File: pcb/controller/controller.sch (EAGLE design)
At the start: 23 parts, among them SW1 EC12E_SW, U1 LCD-16X2NOHOLES

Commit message: Work on controller layout.
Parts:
- removed 3.3V: M01PTH, SparkFun-Connectors:M01PTH
- removed IO1, IO2: (no value), SparkFun-Connectors:M03PTH
- removed POWERLED: (no value), led:LEDSMT1206
- removed S1: CM4400, sensor-comus-group:CM4400
- added BLUETOOTH, JP1, JP2: (no value), SparkFun-Connectors:M041X04_NO_SILK
- added ETHERNET: M05X2NO_SILK, SparkFun-Connectors:M05X2NO_SILK
- added IC1: 74HCT595D, 74xx-eu:74HCT595D
- added JOYSTICK: (no value), SparkFun-Connectors:M05NO_SILK
- added L2: WS2812B, adafruit:WS2812B
- added R2: 1k, rcl:R-EU_M0805
- added R4: 2k, rcl:R-EU_M0805
- added S2, S3: SWITCH-MOMENTARY-2-SMD-1101NE, SparkFun-Electromechanical:SWITCH-MOMENTARY-2-SMD-1101NE
- added VIBRATION_SENSOR: M021X02_NO_SILK, SparkFun-Connectors:M021X02_NO_SILK
- R3: value 100R -> 470R
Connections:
- new net BLUETOOTH_RX: BLUETOOTH.1, R2.1, R4.2
- new net BLUETOOTH_TX: BLUETOOTH.2, U$1.RXI
- new net ETHERNET_CLOCK_OUT: ETHERNET.1
- new net ETHERNET_INT: ETHERNET.2
- new net ETHERNET_RESET: ETHERNET.8
- new net ETHERNET_SELECT: ETHERNET.7, U$1.4
- new net ETHERNET_WDL: ETHERNET.3
- new net LCD_SELECT: IC1A.RCK, U$1.2
- new net PIN3: U$1.*3
- new net PIN5: U$1.*5
- new net PIN6: U$1.*6
- new net PIN7: U$1.7
- new net SERIAL_CLOCK: ETHERNET.6, IC1A.SCK, U$1.13
- new net SERIAL_MISO: ETHERNET.4, U$1.12
- new net SERIAL_MOSI: ETHERNET.5, IC1A.SER, U$1.*11
- new net STATUS_LED2: L1.DOUT, L2.DIN
- net +3V3: now also ETHERNET.9, JP1.3, JP2.3, R3.2; no longer 3.3V.1, POWERLED.A
- net +5V: now also BLUETOOTH.4, IC1A.SCL, IC1P.VCC, JP1.4, JP2.4, L2.VDD; no longer IO1.3, IO2.3
- net EXTRA_IO1: now also JP1.2; no longer IO1.2
- net EXTRA_IO2: now also JP2.2; no longer IO2.2
- net GND: now also BLUETOOTH.3, ETHERNET.10, IC1A.G, IC1P.GND, JP1.1, JP2.1, L2.GND, R4.1, VIBRATION_SENSOR.1; no longer IO1.1, IO2.1, S1.1
- net LCD_DATA4: now also IC1A.QD; no longer U$1.4
- net LCD_DATA5: now also IC1A.QE; no longer U$1.*5
- net LCD_DATA6: now also IC1A.QF; no longer U$1.*6
- net LCD_DATA7: now also IC1A.QG; no longer U$1.7
- net LCD_ENABLE: now also IC1A.QC; no longer U$1.*3
- net LCD_RS: now also IC1A.QB; no longer U$1.2
- net LEDSTRIP_OUT: now also L2.DOUT; no longer L1.DOUT
- net N$1: now also R2.2, U$1.TXO; no longer POWERLED.C, R3.2
- net RADIO_MISO: no longer U$1.12
- net RADIO_MOSI: no longer U$1.*11
- net RADIO_SCK: no longer U$1.13
- net SHAKE_SENSOR: now also VIBRATION_SENSOR.2; no longer S1.2
- net V+: now also U$1.RAW
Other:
- note added: "Bluetooth"
- note added: "Ethernet"
- note added: "NOTE: The regulator needs at least a 10mA load to work, and the radio may draw less than that, so we add an additional pulldown resistor on the 3.3V power rail."
- note added: "Preview LED"
- note removed: "3.3V Out Pin"
- note removed: "NOTE: The regulator needs at least a 10mA load to work, and the radio may draw less than that, so we add the power led on the 3.3V rail."
- note removed: "Status LED"
- moved on the sheet: R1, R3, U1

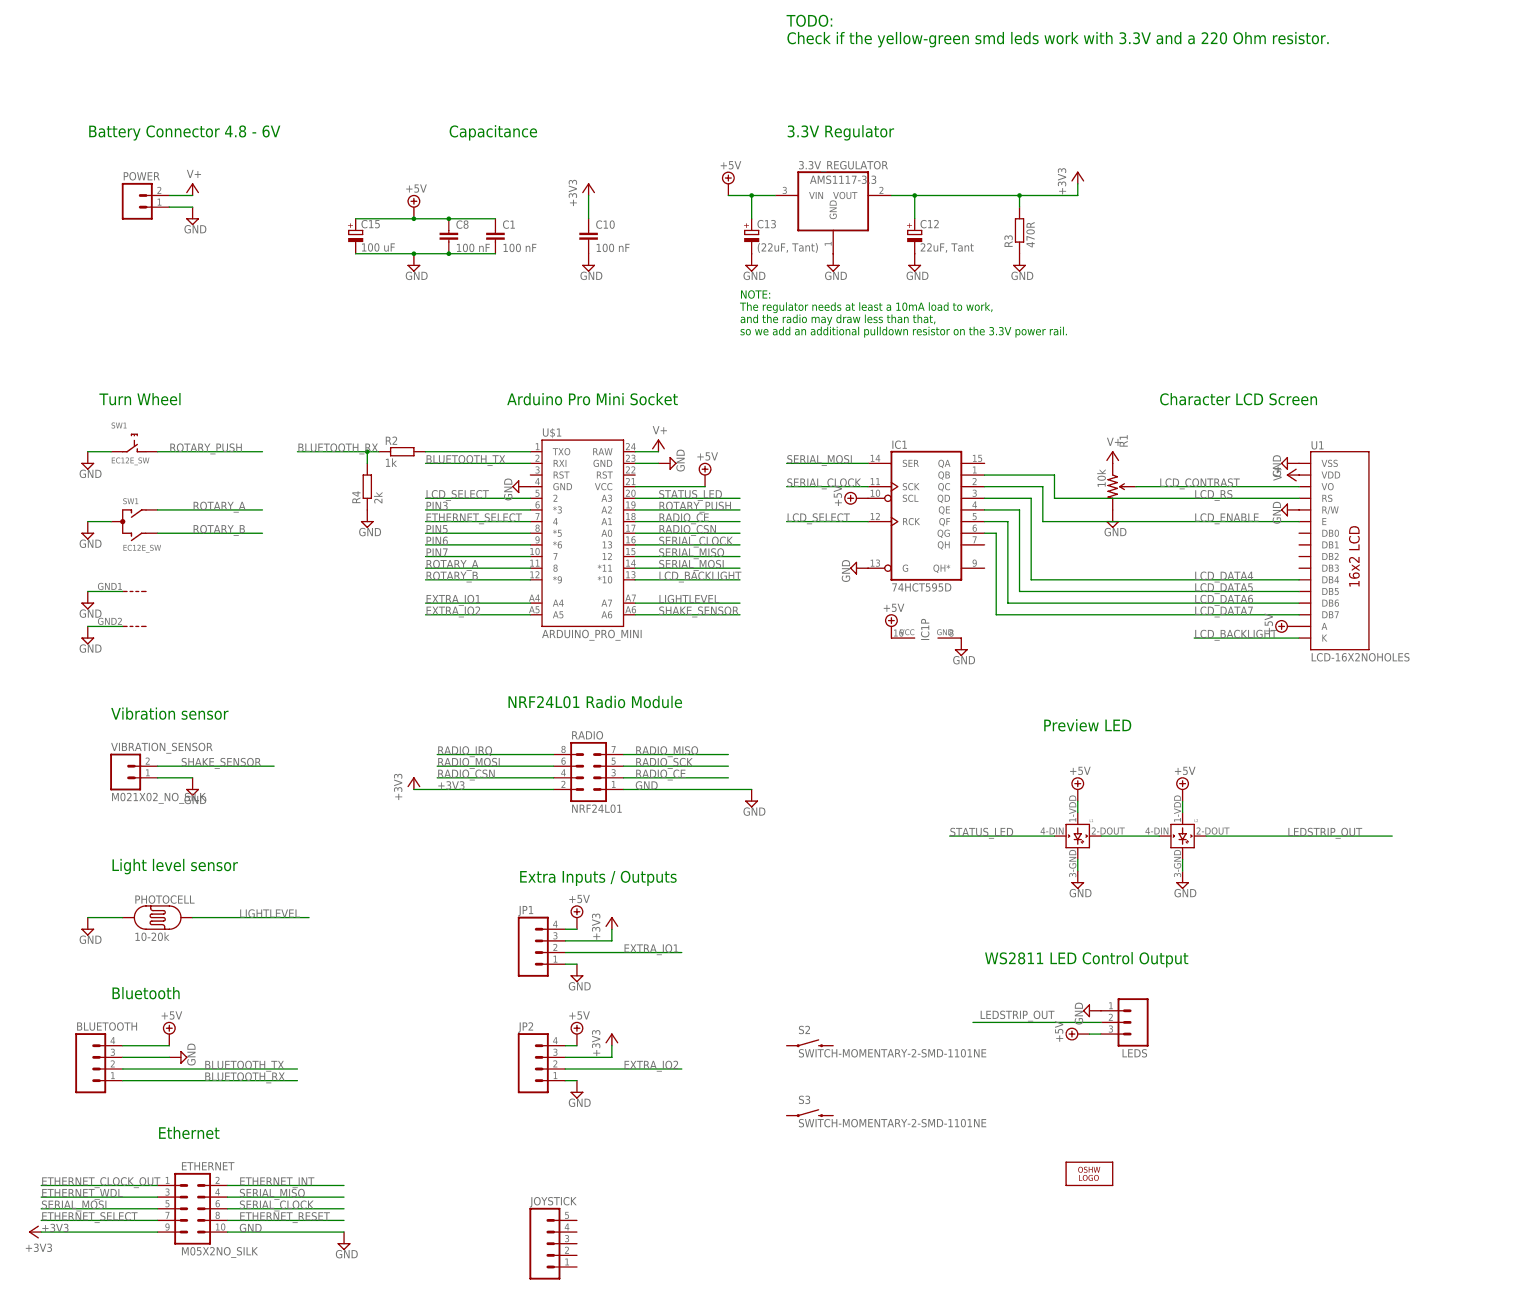
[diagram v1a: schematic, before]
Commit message: Working on remote controller pcb. Added library with connectors and outlines of some of the used third party modules.
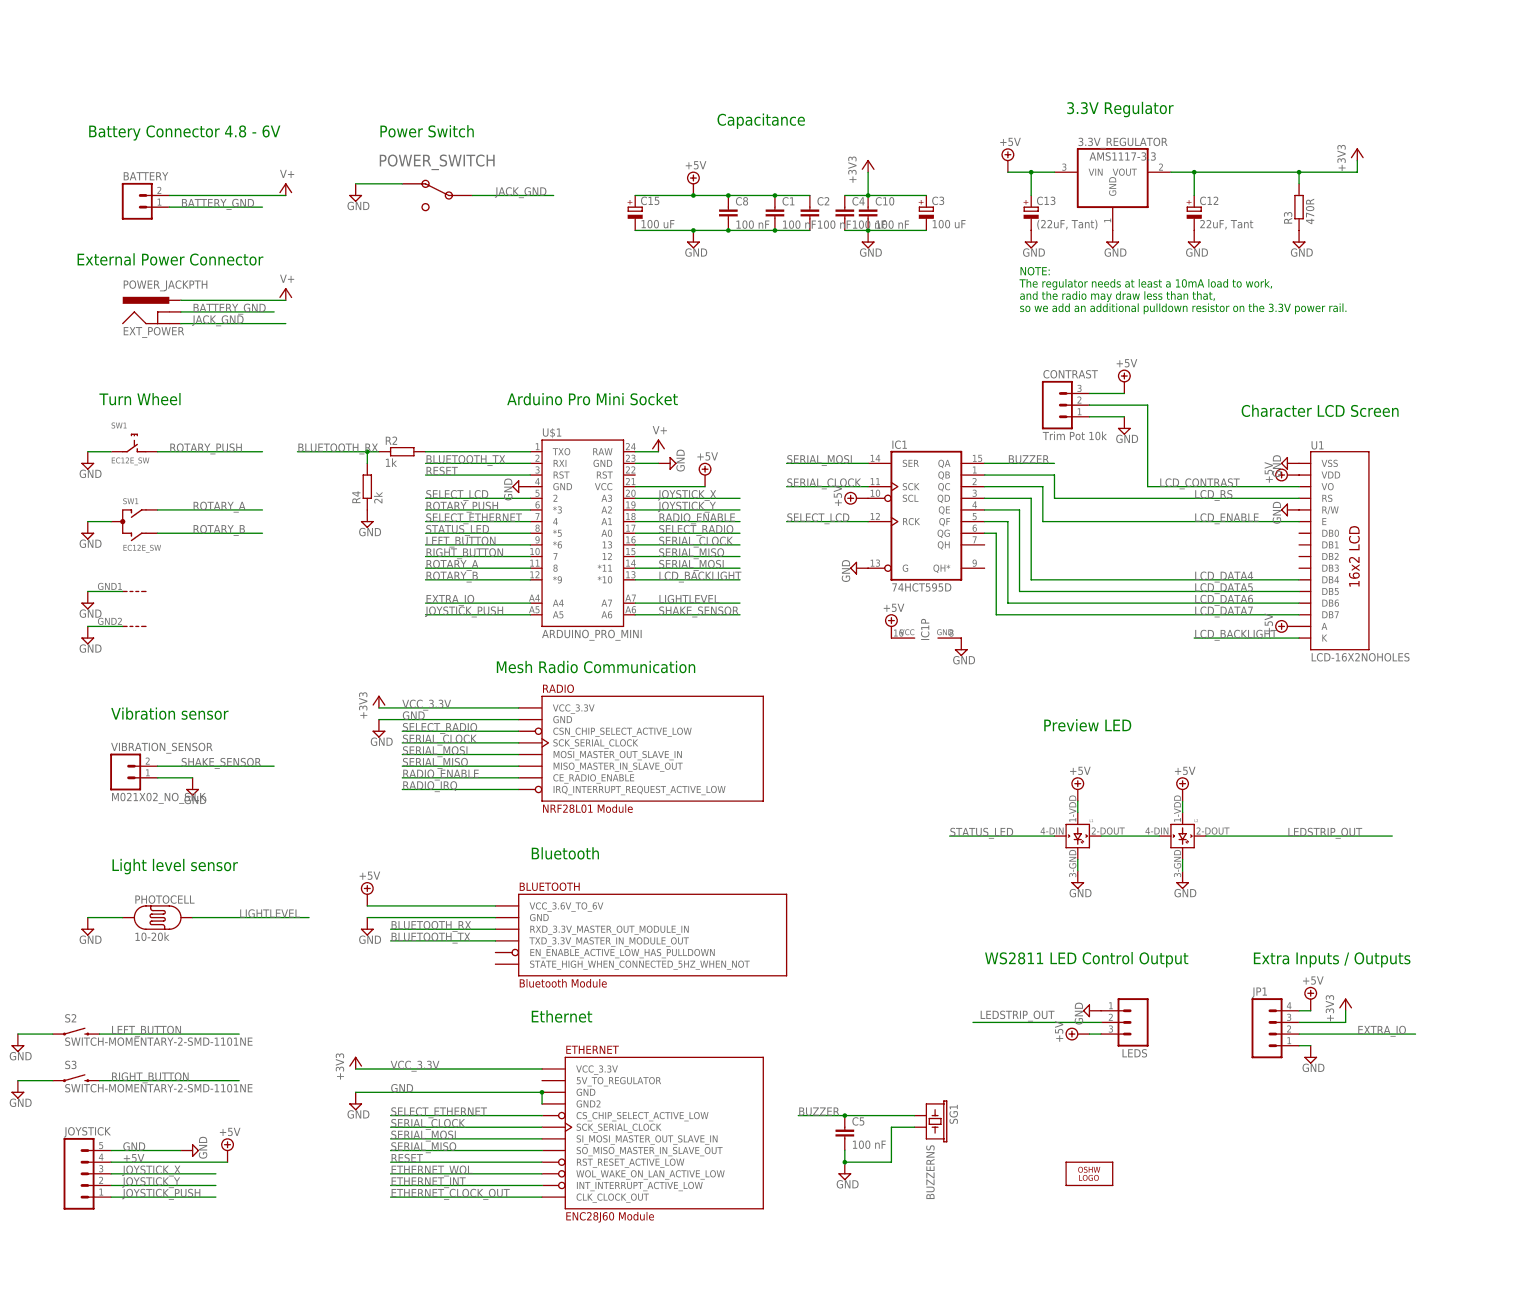
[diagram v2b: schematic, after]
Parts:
- removed JP2: (no value), SparkFun-Connectors:M041X04_NO_SILK
- removed R1: 10k, SparkFun:TRIMPOT
- added C2, C4, C5: 100 nF, rcl:C-EUC0805
- added C3: 100 uF, rcl:CPOL-EUE2.5-6
- added CONTRAST: Trim Pot 10k, SparkFun-Connectors:M031X03_NO_SILK
- added EXT_POWER: POWER_JACKPTH, SparkFun-Connectors:POWER_JACKPTH
- added POWER_SWITCH: KNC1-101-2P, knc1-101-switch:KNC1-101-2P
- added SG1: BUZZERNS, SparkFun-Electromechanical:BUZZERNS
- BLUETOOTH: value (none) -> Bluetooth Module; device SparkFun-Connectors:M041X04_NO_SILK -> common_modules:BLUETOOTH_MODULE
- ETHERNET: value M05X2NO_SILK -> ENC28J60 Module; device SparkFun-Connectors:M05X2NO_SILK -> common_modules:ETHERNET_ENC28J60_MODULE
- RADIO: value NRF24L01 -> NRF28L01 Module; device con-lstb:MA04-2 -> common_modules:NRF24L01_MODULE
- renumbered POWER to BATTERY
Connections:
- net EXTRA_IO1 renamed EXTRA_IO
- net LCD_SELECT renamed SELECT_LCD
- removed net ETHERNET_RESET: ETHERNET.8
- removed net ETHERNET_SELECT: ETHERNET.7, U$1.4
- removed net ETHERNET_WDL: ETHERNET.3
- removed net EXTRA_IO2: JP2.2, U$1.A5
- removed net PIN3: U$1.*3
- removed net PIN5: U$1.*5
- removed net PIN6: U$1.*6
- removed net PIN7: U$1.7
- removed net RADIO_CE: RADIO.3, U$1.A1
- removed net RADIO_CSN: RADIO.4, U$1.A0
- removed net RADIO_MISO: RADIO.7
- removed net RADIO_MOSI: RADIO.6
- removed net RADIO_SCK: RADIO.5
- new net BATTERY_GND: BATTERY.1, EXT_POWER.GNDBREAK
- new net BUZZER: C5.1, IC1A.QA, SG1.1
- new net ETHERNET_WOL: ETHERNET.WOL_WAKE_ON_LAN_ACTIVE_LOW
- new net JACK_GND: EXT_POWER.GND, POWER_SWITCH.P$2
- new net JOYSTICK_PUSH: JOYSTICK.1, U$1.A5
- new net JOYSTICK_X: JOYSTICK.3, U$1.A3
- new net JOYSTICK_Y: JOYSTICK.2, U$1.A2
- new net LEFT_BUTTON: S2.2, U$1.*6
- new net RADIO_ENABLE: RADIO.CE_RADIO_ENABLE, U$1.A1
- new net RESET: ETHERNET.RST_RESET_ACTIVE_LOW, U$1.RST
- new net RIGHT_BUTTON: S3.2, U$1.7
- new net SELECT_ETHERNET: ETHERNET.CS_CHIP_SELECT_ACTIVE_LOW, U$1.4
- new net SELECT_RADIO: RADIO.CSN_CHIP_SELECT_ACTIVE_LOW, U$1.A0
- new net VCC_3.3V: ETHERNET.VCC_3.3V, RADIO.VCC_3.3V
- net +3V3: now also C3.+, C4.1; no longer ETHERNET.9, JP2.3, RADIO.2
- net +5V: now also BLUETOOTH.VCC_3.6V_TO_6V, C2.1, CONTRAST.3, JOYSTICK.4, U1.VDD; no longer BLUETOOTH.4, JP2.4
- net BLUETOOTH_RX: now also BLUETOOTH.RXD_3.3V_MASTER_OUT_MODULE_IN; no longer BLUETOOTH.1
- net BLUETOOTH_TX: now also BLUETOOTH.TXD_3.3V_MASTER_IN_MODULE_OUT; no longer BLUETOOTH.2
- net ETHERNET_CLOCK_OUT: now also ETHERNET.CLK_CLOCK_OUT; no longer ETHERNET.1
- net ETHERNET_INT: now also ETHERNET.INT_INTERRUPT_ACTIVE_LOW; no longer ETHERNET.2
- net GND: now also BLUETOOTH.GND, C2.2, C3.-, C4.2, C5.2, CONTRAST.1, ETHERNET.GND, ETHERNET.GND2, JOYSTICK.5, POWER_SWITCH.P$1, RADIO.GND, S2.1, S3.1, SG1.2; no longer BATTERY.1, BLUETOOTH.3, ETHERNET.10, JP2.1, R1.CW, RADIO.1
- net LCD_CONTRAST: now also CONTRAST.2; no longer R1.WIPER
- net RADIO_IRQ: now also RADIO.IRQ_INTERRUPT_REQUEST_ACTIVE_LOW; no longer RADIO.8
- net ROTARY_PUSH: now also U$1.*3; no longer U$1.A2
- net SERIAL_CLOCK: now also ETHERNET.SCK_SERIAL_CLOCK, RADIO.SCK_SERIAL_CLOCK; no longer ETHERNET.6
- net SERIAL_MISO: now also ETHERNET.SO_MISO_MASTER_IN_SLAVE_OUT, RADIO.MISO_MASTER_IN_SLAVE_OUT; no longer ETHERNET.4
- net SERIAL_MOSI: now also ETHERNET.SI_MOSI_MASTER_OUT_SLAVE_IN, RADIO.MOSI_MASTER_OUT_SLAVE_IN; no longer ETHERNET.5
- net STATUS_LED: now also U$1.*5; no longer U$1.A3
- net V+: now also EXT_POWER.PWR; no longer R1.CCW, U1.VDD
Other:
- note added: "External Power Connector"
- note added: "Mesh Radio Communication"
- note added: "Power Switch"
- note removed: "NRF24L01 Radio Module"
- note removed: "TODO: Check if the yellow-green smd leds work with 3.3V and a 220 Ohm resistor."
- moved on the sheet: 3.3V_REGULATOR, C1, C10, C12, C13, C15, C8, JOYSTICK, JP1, R3, S2, S3

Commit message: Working on routing.
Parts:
- removed C4: 100 nF, rcl:C-EUC0805
- added EXTRA_OUT: M02PTH, SparkFun-Connectors:M02PTH
- C15, C3: value 100 uF -> 10 uF; device rcl:CPOL-EUE2.5-6 -> rcl:C-EUC0805K
- R3: value 470R -> (470R)
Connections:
- removed net +3V3: 3.3V_REGULATOR.VOUT, C10.1, C12.+, C3.+, C4.1, JP1.3, R3.2
- removed net VCC_3.3V: ETHERNET.VCC_3.3V, RADIO.VCC_3.3V
- new net +3.3V: 3.3V_REGULATOR.VOUT, C10.1, C12.+, C3.1, ETHERNET.VCC_3.3V, JP1.3, R3.2, RADIO.VCC_3.3V
- new net EXTRA_OUTPUT: EXTRA_OUT.1, IC1A.QH
- net +5V: now also C15.1; no longer C15.+
- net GND: now also C15.2, C3.2, EXTRA_OUT.2; no longer C15.-, C3.-, C4.2
- net LCD_ENABLE: now also IC1A.QB; no longer IC1A.QC
- net LCD_RS: now also IC1A.QC; no longer IC1A.QB
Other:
- note added: "NOTE: The regulator needs at least a 10mA load to work, and the radio may draw less than that, so we add an optional pulldown resistor on the 3.3V power rail."
- note removed: "NOTE: The regulator needs at least a 10mA load to work, and the radio may draw less than that, so we add an additional pulldown resistor on the 3.3V power rail."
